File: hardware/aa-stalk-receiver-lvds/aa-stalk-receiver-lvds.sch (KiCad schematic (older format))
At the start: 65 parts, among them CN101 Conn_01x02, CN102 6P6C, CN151 Conn_01x04, CN301 Conn_01x03, CN302 Conn_01x03, CN303 Conn_01x03, CN311 Conn_01x02, CN312 Conn_01x02, CN313 Conn_01x02, CN314 Conn_01x02, Q301 KST10, Q311 MCH3484, Q312 MCH3484, U201 ST26C32

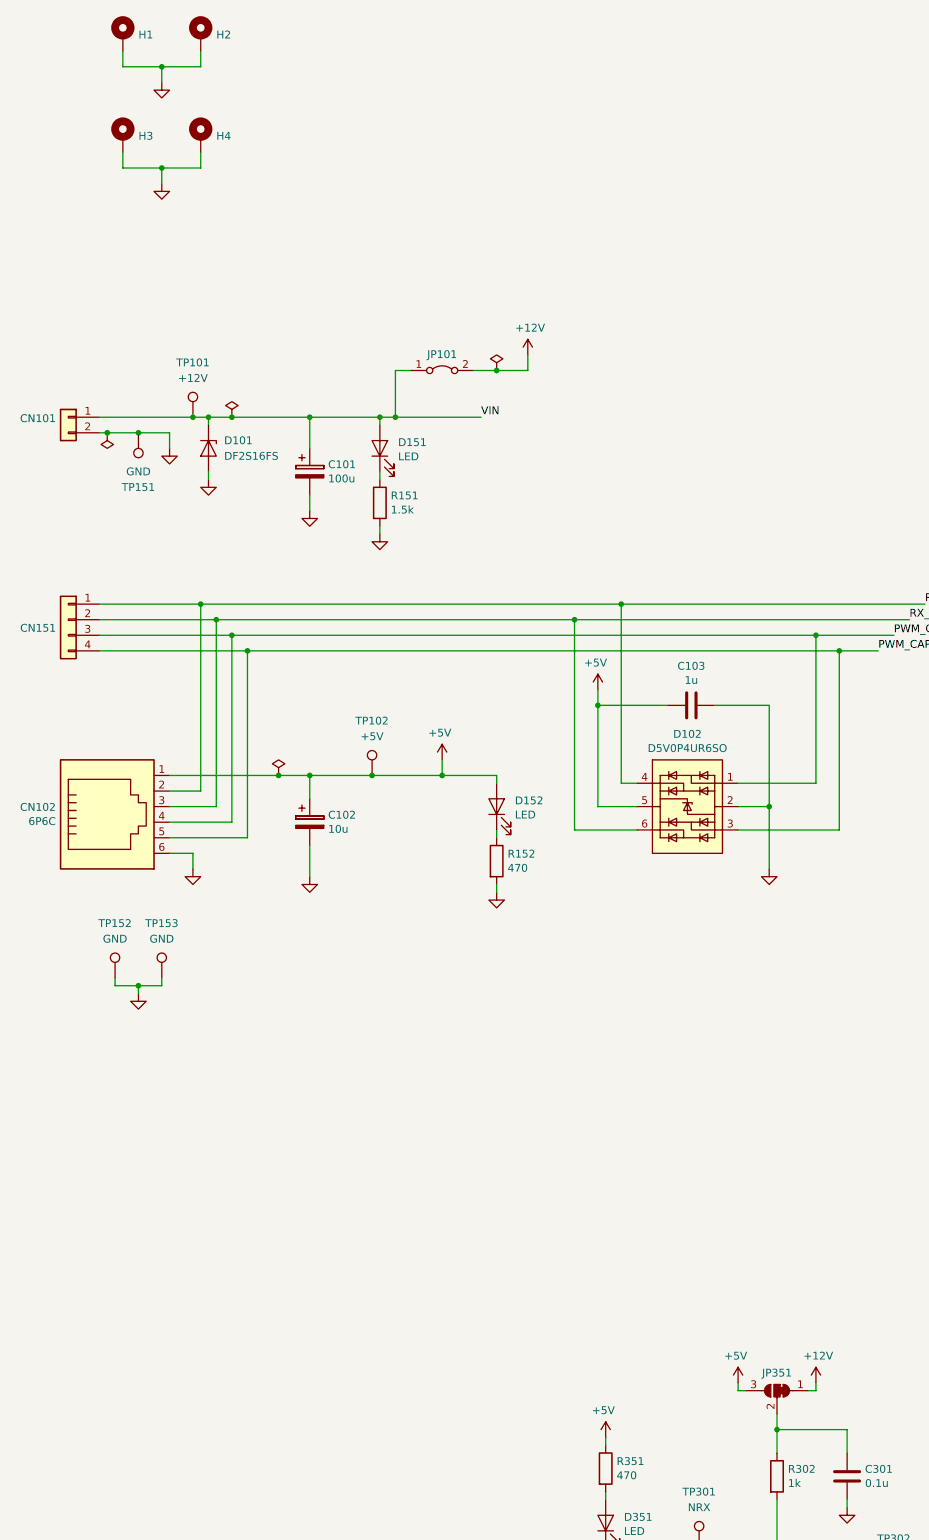
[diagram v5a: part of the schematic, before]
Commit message: Final designs and actual sent gerbers for first for-real run
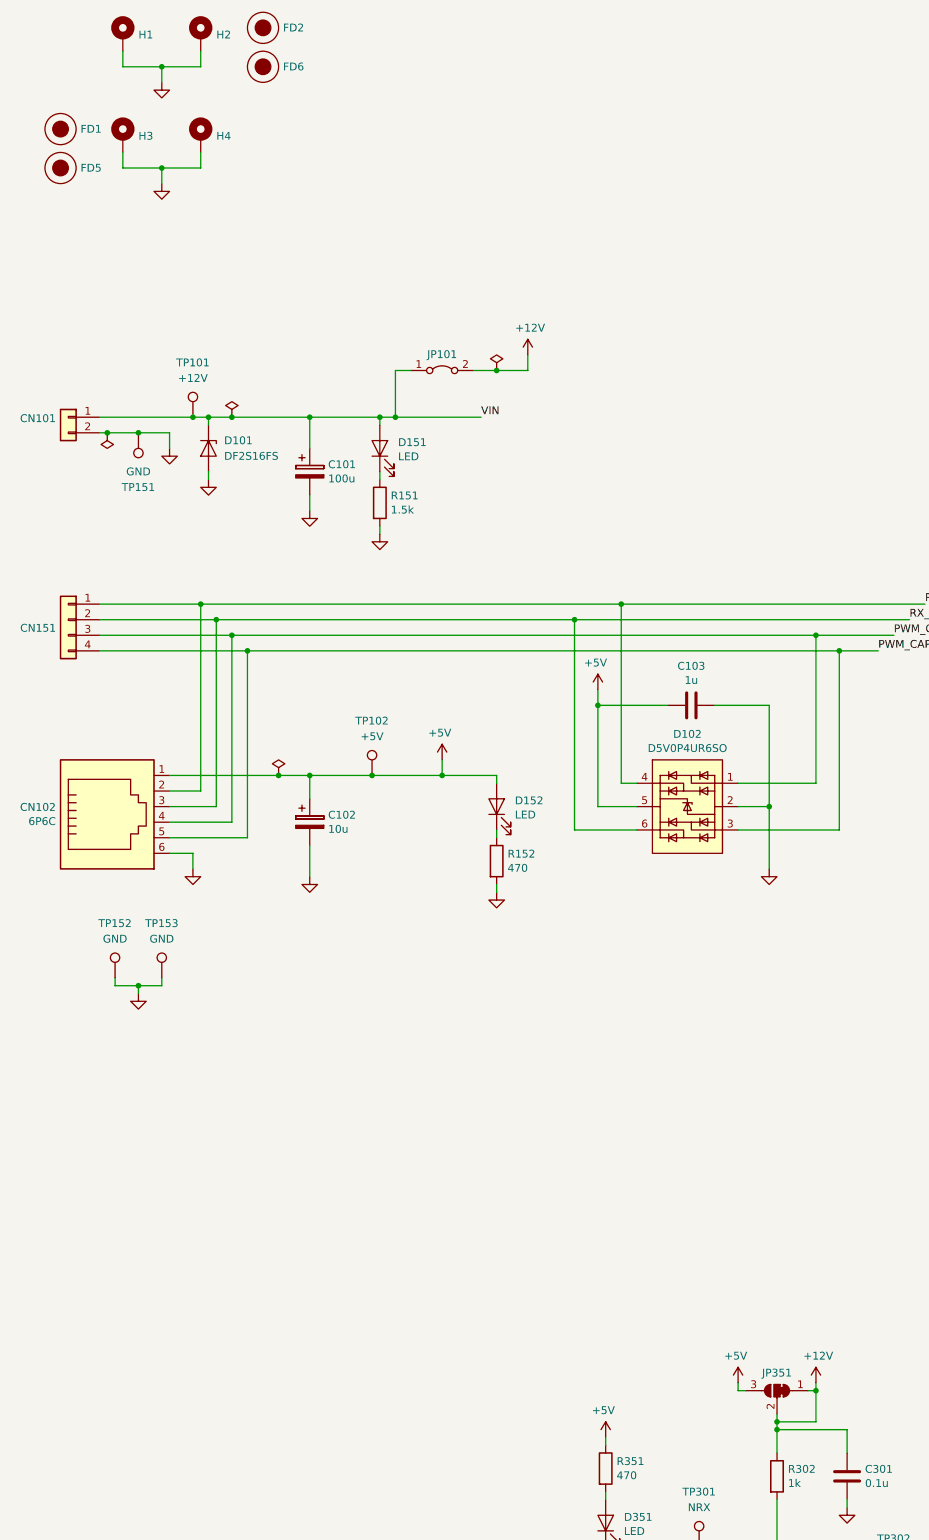
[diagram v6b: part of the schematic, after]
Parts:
- added FD1, FD2: Fiducial, Fiducial:Fiducial_1mm_Dia_2.54mm_Outer_CopperTop, symbol aa-shared:Fiducial
- added FD5, FD6: Fiducial, aa-shared:StencilAlignment_1.27mm, symbol aa-shared:Fiducial
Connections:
- net +12V: now also C301.1, JP351.2 (C), R302.1
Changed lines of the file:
@@
 	8350 10650 8350 10600
 Wire Wire Line
-	8600 10800 8600 10900
+	8600 10800 8600 10850
 $Comp
 L power:GND #PWR026
@@
 Wire Wire Line
 	6000 6700 6450 6700
+Wire Wire Line
+	8850 10650 8850 10850
+Wire Wire Line
+	8850 10850 8600 10850
+Connection ~ 8850 10650
+Connection ~ 8600 10850
+Wire Wire Line
+	8600 10850 8600 10900
+$Comp
+L aa-shared:Fiducial FD1
+U 1 1 5D0F3C4F
+P 4000 2550
+F 0 "FD1" H 4128 2550 50  0000 L CNN
+F 1 "Fiducial" H 4000 2700 50  0001 C CNN
+F 2 "Fiducial:Fiducial_1mm_Dia_2.54mm_Outer_CopperTop" H 4000 2550 50  0001 C CNN
+F 3 "" H 4000 2550 50  0001 C CNN
+	1    4000 2550
+	1    0    0    -1
+$EndComp
+$Comp
+L aa-shared:Fiducial FD2
+U 1 1 5D0F3D0F
+P 5300 1900
+F 0 "FD2" H 5428 1900 50  0000 L CNN
+F 1 "Fiducial" H 5300 2050 50  0001 C CNN
+F 2 "Fiducial:Fiducial_1mm_Dia_2.54mm_Outer_CopperTop" H 5300 1900 50  0001 C CNN
+F 3 "" H 5300 1900 50  0001 C CNN
+	1    5300 1900
+	1    0    0    -1
+$EndComp
+$Comp
+L aa-shared:Fiducial FD5
+U 1 1 5D0F3DE5
+P 4000 2800
+F 0 "FD5" H 4128 2800 50  0000 L CNN
+F 1 "Fiducial" H 4000 2950 50  0001 C CNN
+F 2 "aa-shared:StencilAlignment_1.27mm" H 4000 2800 50  0001 C CNN
+F 3 "" H 4000 2800 50  0001 C CNN
+	1    4000 2800
+	1    0    0    -1
+$EndComp
+$Comp
+L aa-shared:Fiducial FD6
+U 1 1 5D0F3EB3
+P 5300 2150
+F 0 "FD6" H 5428 2150 50  0000 L CNN
+F 1 "Fiducial" H 5300 2300 50  0001 C CNN
+F 2 "aa-shared:StencilAlignment_1.27mm" H 5300 2150 50  0001 C CNN
+F 3 "" H 5300 2150 50  0001 C CNN
+	1    5300 2150
+	1    0    0    -1
+$EndComp
 $EndSCHEMATC

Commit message: Second run of PCBs for Amanita Arcade
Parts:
- D102: value D5V0P4UR6SO -> DS1042
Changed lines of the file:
@@
 P 8050 6900
 F 0 "D102" H 8075 7365 50  0000 C CNN
-F 1 "D5V0P4UR6SO" H 8075 7274 50  0000 C CNN
+F 1 "DS1042" H 8075 7274 50  0000 C CNN
 F 2 "Package_TO_SOT_SMD:SOT-23-6" H 7500 6500 50  0001 L CNN
 F 3 "" V 8175 6775 50  0001 C CNN

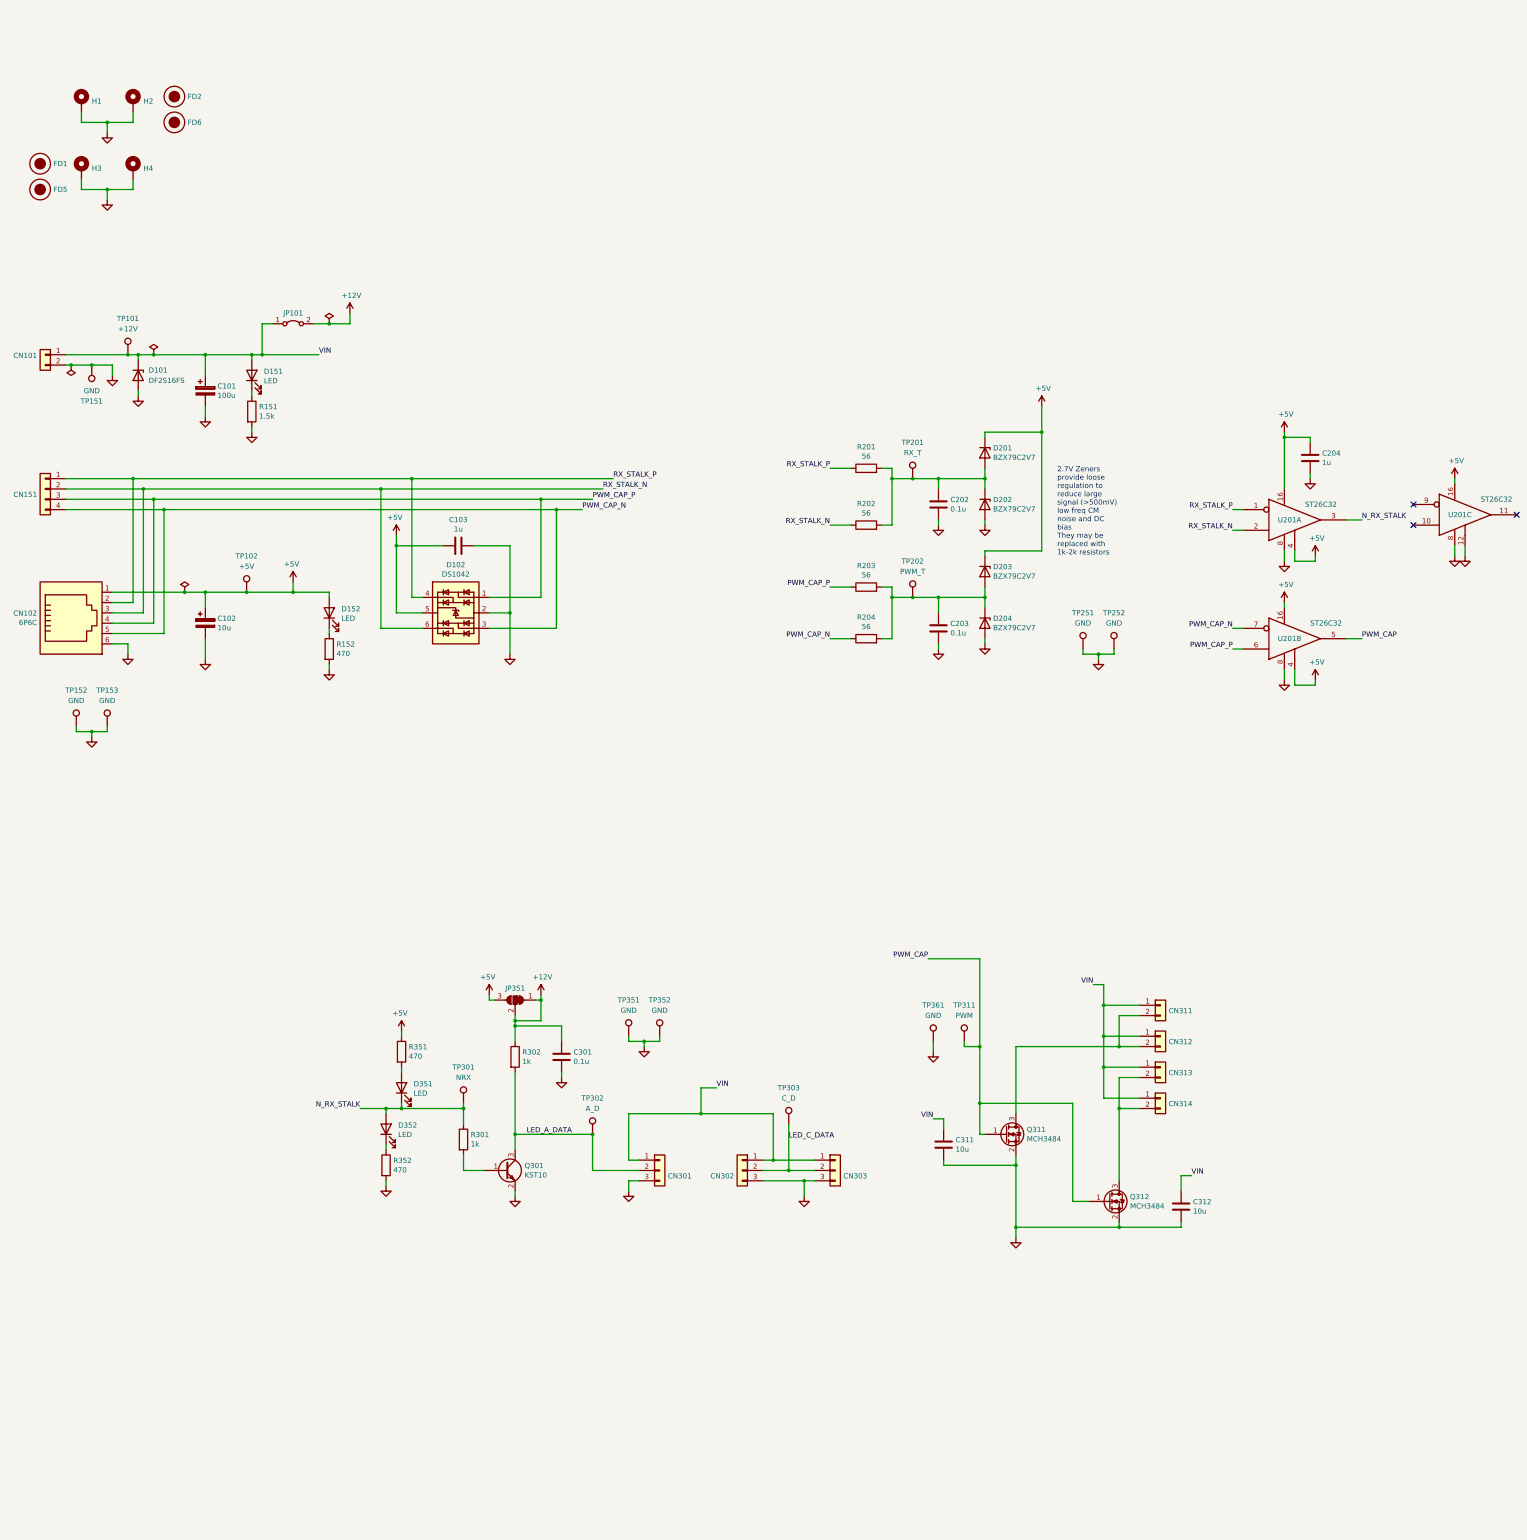
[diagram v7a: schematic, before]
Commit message: Minor board updates to fix issues discovered during build
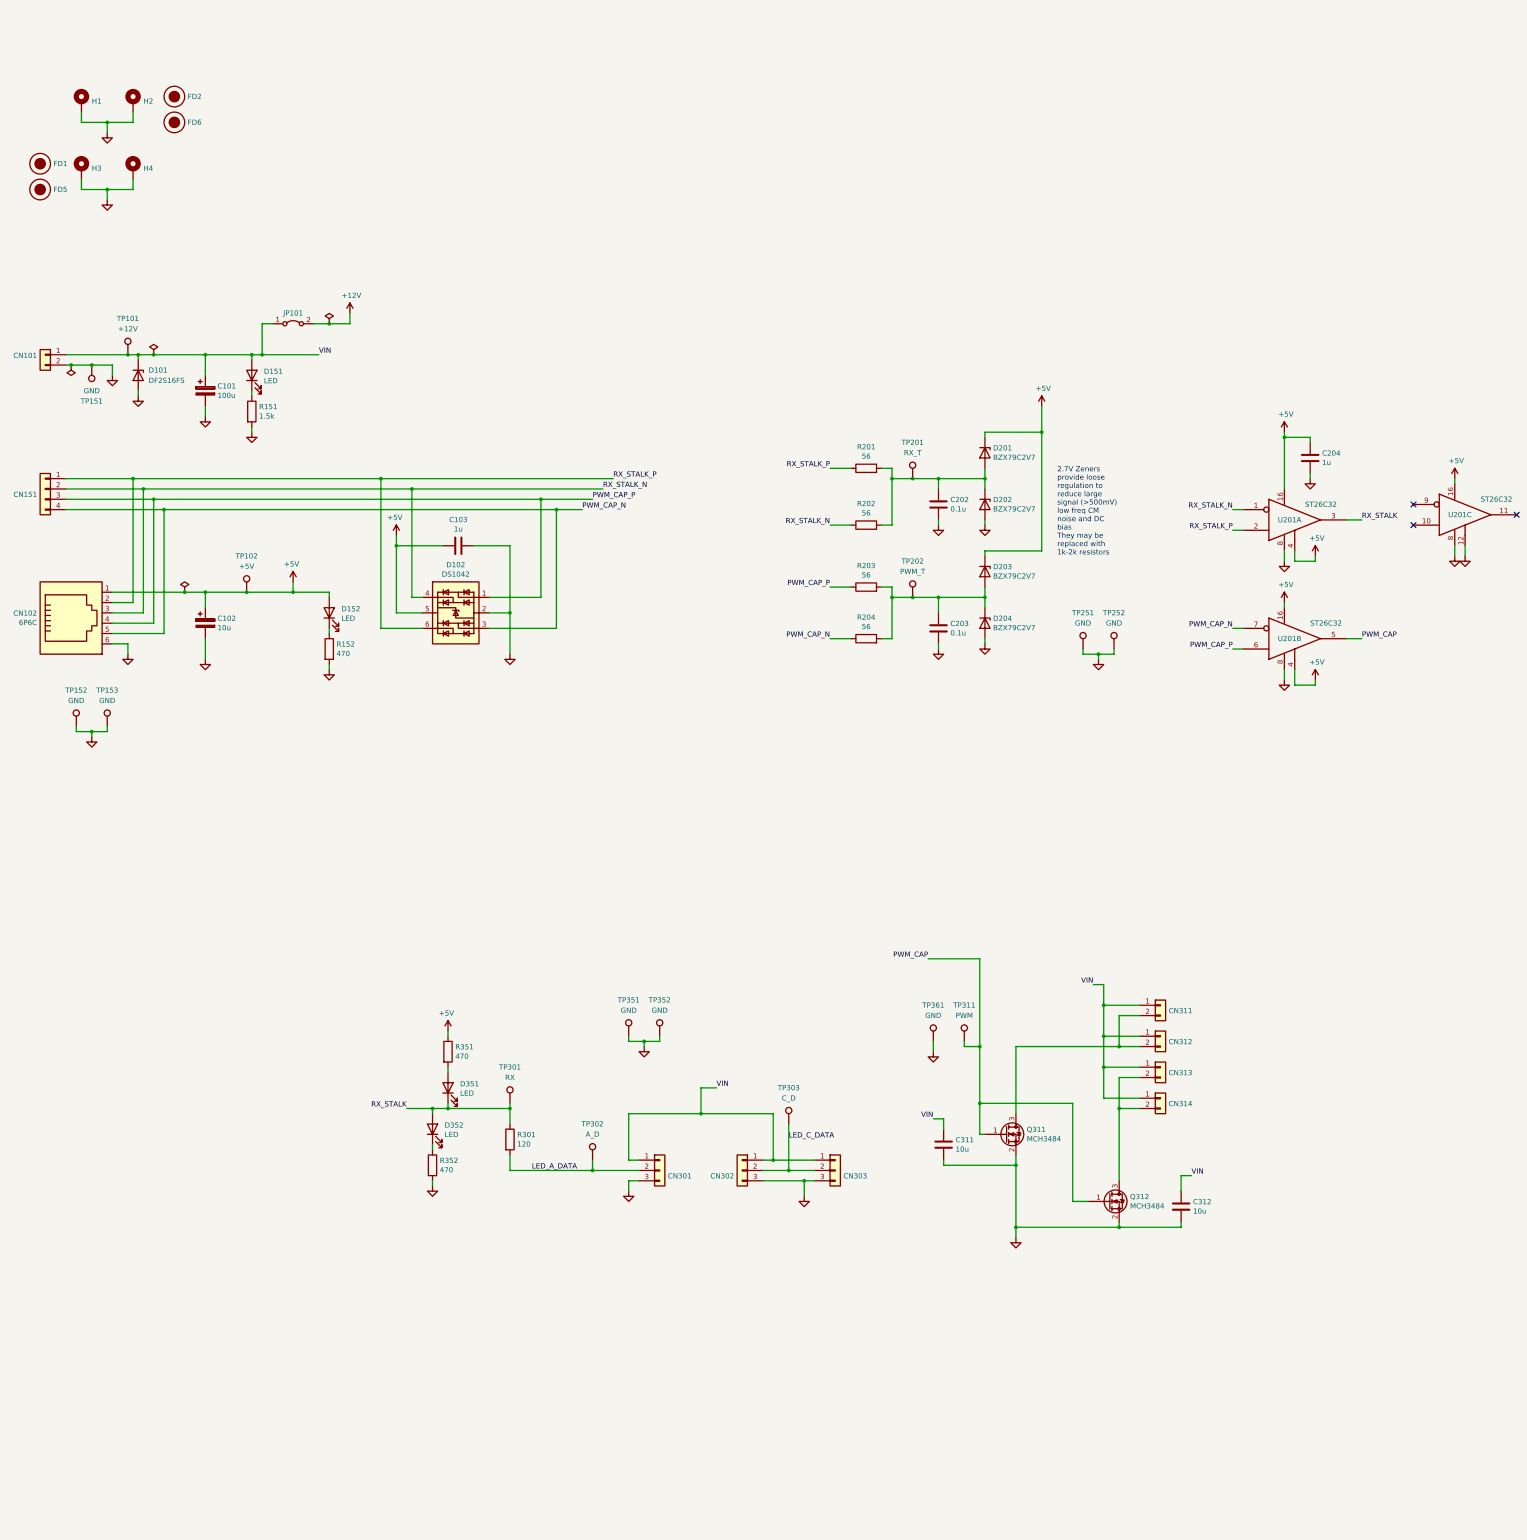
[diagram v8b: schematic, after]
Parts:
- removed C301: 0.1u, Capacitor_SMD:C_0805_2012Metric, symbol Device:C
- removed JP351: SolderJumper_3_Bridged12, Jumper:SolderJumper-3_P1.3mm_Open_RoundedPad1.0x1.5mm, symbol Jumper:SolderJumper_3_Bridged12
- removed Q301: KST10, Package_TO_SOT_SMD:SOT-23, symbol Device:Q_NPN_BEC
- removed R302: 1k, Resistor_SMD:R_0603_1608Metric, symbol Device:R
- R301: value 1k -> 120
- TP301: value NRX -> RX
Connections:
- net LED_A_DATA: now also R301.2
- net RX_STALK_N: now also D102.4 (K), U201.1 (E-); no longer D102.6 (K), U201.2 (E+)
- net RX_STALK_P: now also D102.6 (K), U201.2 (E+); no longer D102.4 (K), U201.1 (E-)
- net N_RX_STALK renamed RX_STALK
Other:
- moved on the sheet: D351, D352, R301, R351, R352, TP301, TP302
